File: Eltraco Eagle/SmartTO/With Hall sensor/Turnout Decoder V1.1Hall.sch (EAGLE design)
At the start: 72 parts, among them K1 NA, K2 NA, T1 BC547, T2 BC547, T3 BC547, T4 BC547

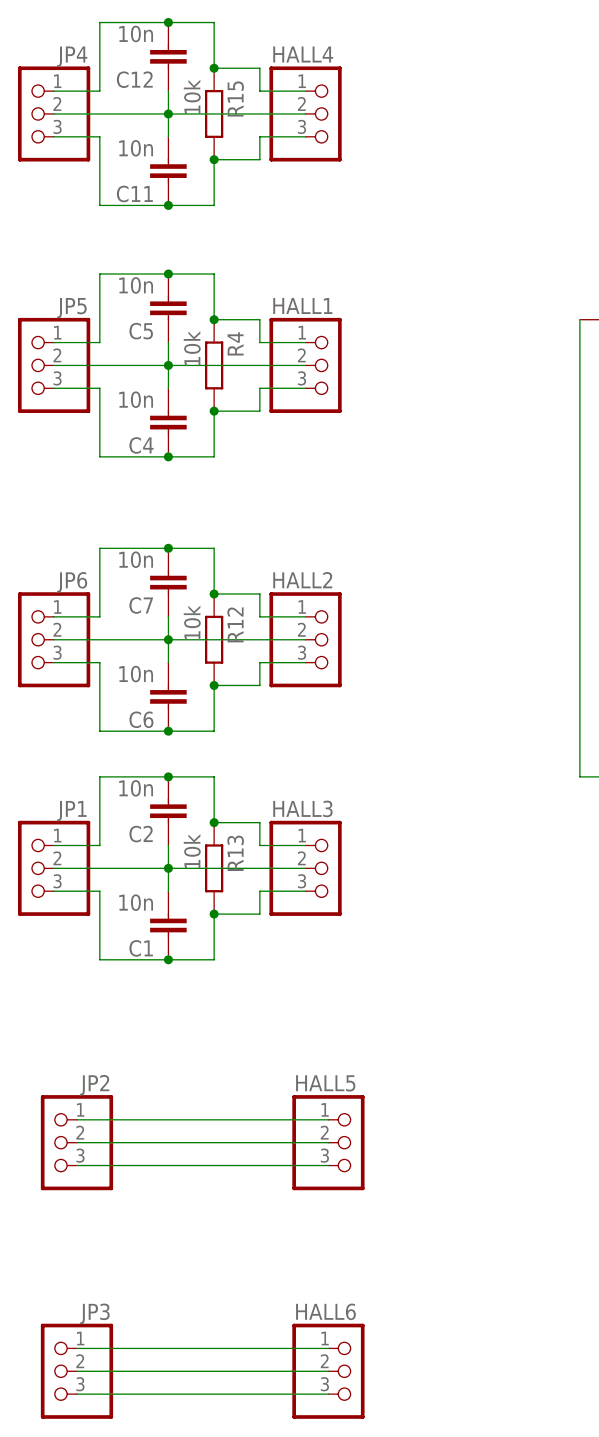
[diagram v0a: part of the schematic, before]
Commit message: New version PCB files and extra PCBs
Value of components printed on PCB. Current sensor, hall sensor and
relais add-on PCB added
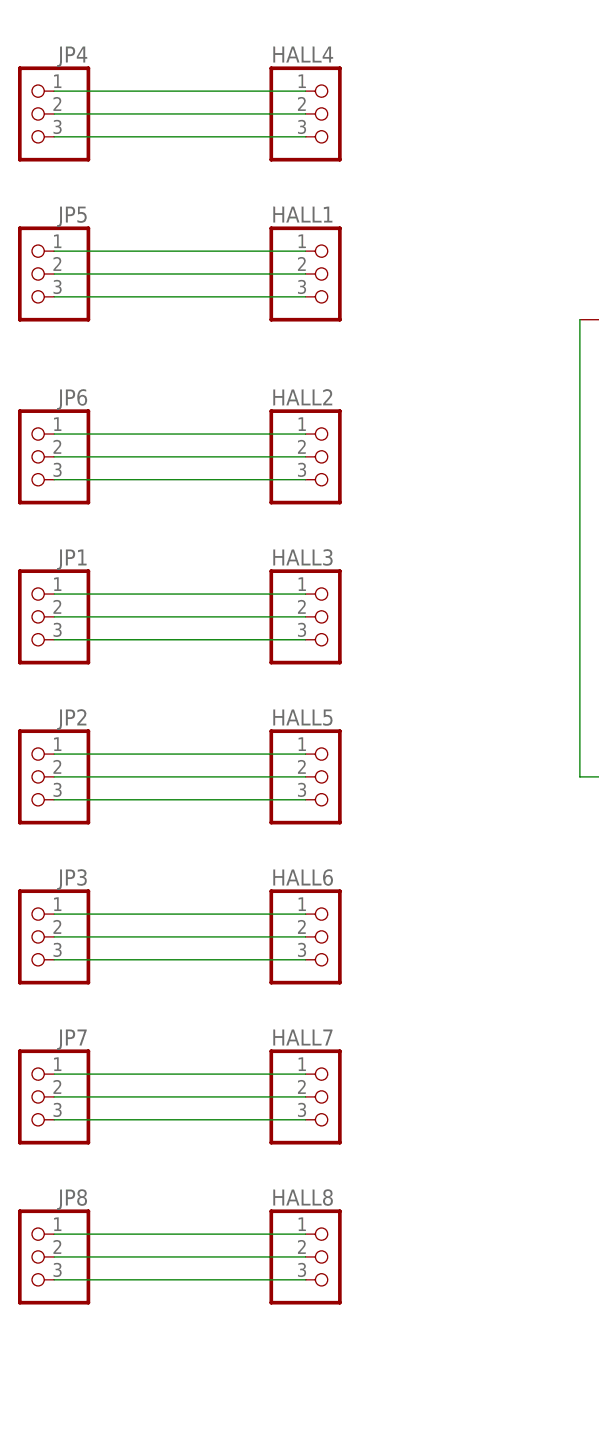
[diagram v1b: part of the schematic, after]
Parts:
- removed C1, C11, C12, C2, C4, C5, C6, C7: 10n, resistor:C-EU050-024X044
- removed R12, R13, R15, R4: 10k, resistor:R-EU_0309/10
- added HALL7, HALL8, JP7, JP8: (no value), pinhead:PINHD-1X3
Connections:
- new net N$52: HALL7.2, JP7.2
- new net N$53: HALL7.1, JP7.1
- new net N$54: HALL7.3, JP7.3
- new net N$59: HALL8.2, JP8.2
- new net N$60: HALL8.1, JP8.1
- new net N$61: HALL8.3, JP8.3
- net N$1: no longer C4.2, C5.1
- net N$24: no longer C5.2, R4.1
- net N$25: no longer C4.1, R4.2
- net N$30: no longer C6.2, C7.1
- net N$36: no longer C7.2, R12.1
- net N$37: no longer C6.1, R12.2
- net N$38: no longer C1.2, C2.1
- net N$39: no longer C2.2, R13.1
- net N$40: no longer C1.1, R13.2
- net N$55: no longer C11.2, C12.1
- net N$56: no longer C11.1, R15.2
- net N$57: no longer C12.2, R15.1
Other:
- moved on the sheet: HALL1, HALL2, HALL3, HALL5, HALL6, JP1, JP2, JP3, JP5, JP6
